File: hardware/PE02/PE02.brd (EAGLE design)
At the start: 25.4 x 27.3 mm, 28 parts, among them IC1 MSP430G2231, IC2 TPS78222, J1 78171-0002

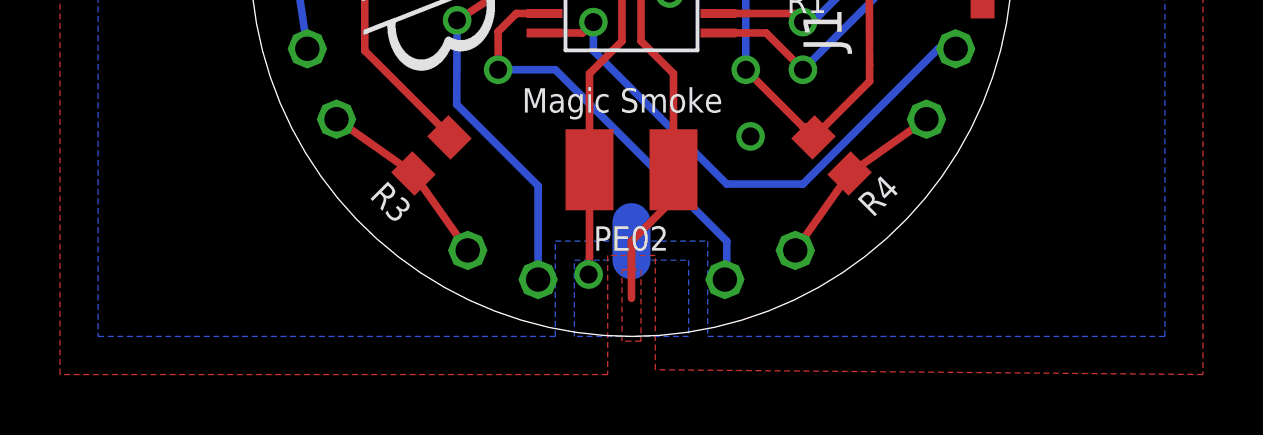
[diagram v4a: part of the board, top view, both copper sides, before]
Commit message: fixed stop mask on battery tab pads
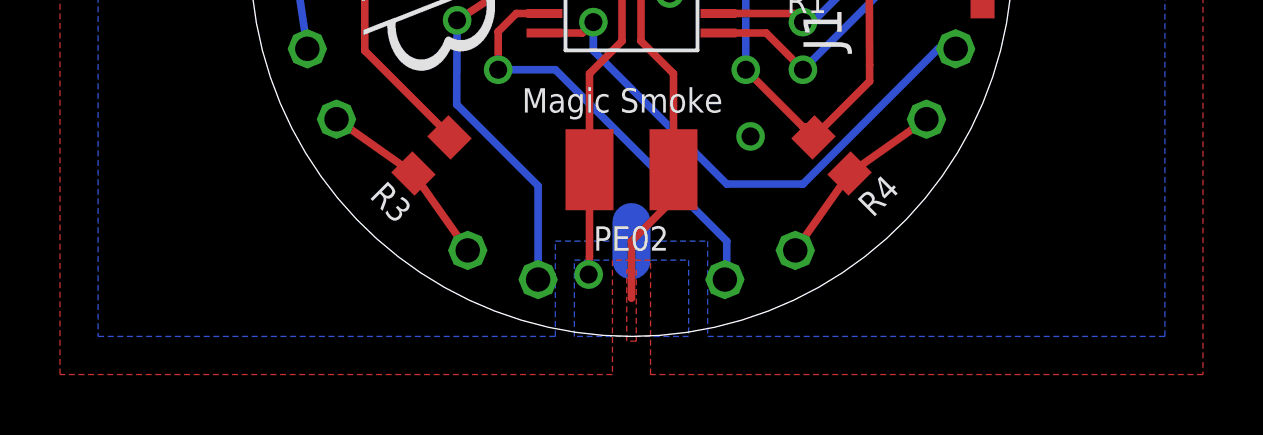
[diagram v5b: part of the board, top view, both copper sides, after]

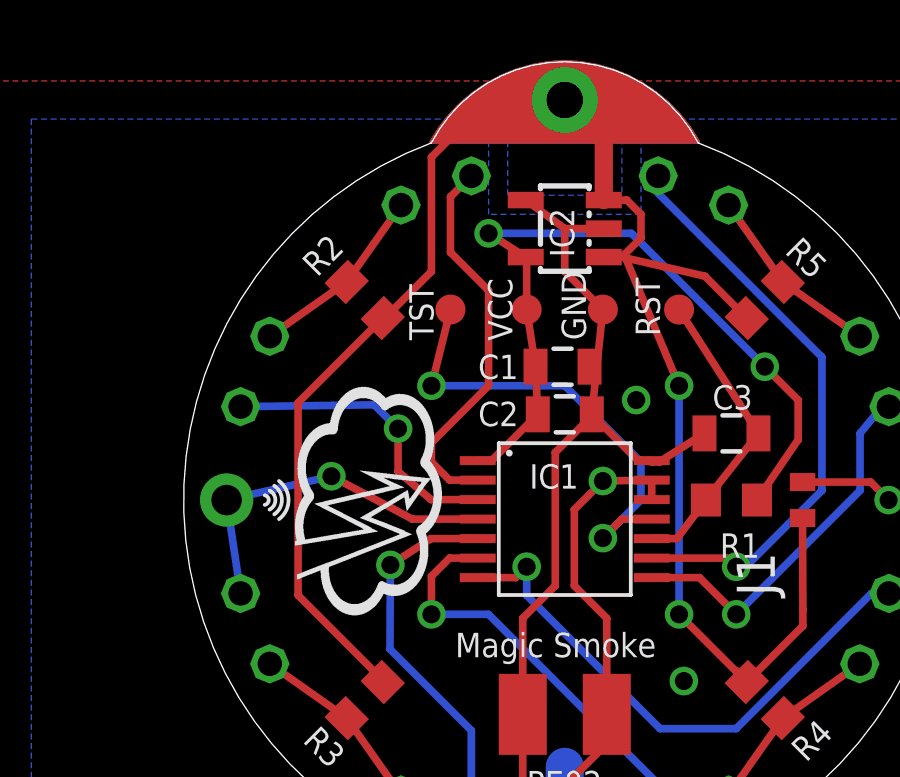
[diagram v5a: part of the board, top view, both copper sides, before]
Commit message: removed sewtab, buzzer hole
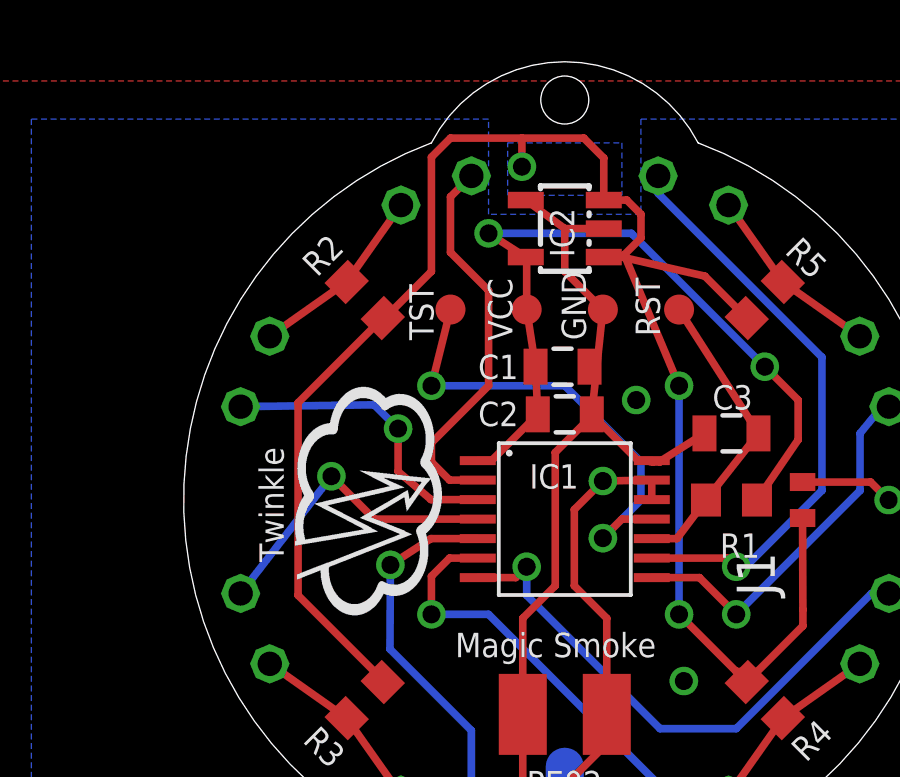
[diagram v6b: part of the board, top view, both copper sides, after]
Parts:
- removed JP1: BUZZER, adafruit:1X01-CLEANBIG
- removed TP1, TP2: SEWTAP0.4IN, adafruit:SEWINGTAP_0.4
- moved U$1 0.32 mm to (50.8, 48.6)
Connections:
- removed net N$6: D3.K, IC1.4, JP1.1
- new net N$7: D3.K, IC1.4
- net V+: no longer TP1.TAP, TP2.TAP
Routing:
- net N$6: track 12.0 -> 0.00 mm, vias 1 -> 0
- net N$7: track 0.00 -> 10.4 mm, vias 0 -> 1
- net V+: track 60.6 -> 60.1 mm, vias 2 -> 3
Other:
- board text added: "Twinkle"
- board text removed: "Magic"
- board text removed: "Smoke"
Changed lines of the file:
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@@
 <plain>
 <circle x="50.8" y="55.88" radius="11.43" width="0.0254" layer="48"/>
-<wire x1="40.79875" y1="55.72125" x2="40.79875" y2="56.03875" width="0.127" layer="21" curve="160"/>
-<wire x1="40.9575" y1="55.5625" x2="40.9575" y2="56.1975" width="0.127" layer="21" curve="126.869898"/>
-<wire x1="41.11625" y1="55.40375" x2="41.11625" y2="56.35625" width="0.127" layer="21" curve="112.619865"/>
-<wire x1="41.275" y1="55.245" x2="41.275" y2="56.515" width="0.127" layer="21" curve="106.260205"/>
 <text x="47.14875" y="50.64125" size="0.8128" layer="21" font="vector" ratio="15">Magic Smoke</text>
-<text x="59.3725" y="62.07125" size="0.8128" layer="22" font="vector" ratio="15" rot="MR45">Magic</text>
-<text x="44.60875" y="64.4525" size="0.8128" layer="22" font="vector" ratio="15" rot="MR315">Smoke</text>
 <text x="54.9275" y="50.64125" size="0.8128" layer="22" font="vector" ratio="15" rot="MR0">CC BY-SA 3.0</text>
 <circle x="50.8" y="55.88" radius="9.939321875" width="0.0254" layer="52"/>
@@
 <rectangle x1="50.32375" y1="43.4975" x2="51.27625" y2="45.56125" layer="29"/>
 <rectangle x1="48.73625" y1="43.4975" x2="52.86375" y2="45.87875" layer="30"/>
-<rectangle x1="48.73625" y1="65.88125" x2="52.86375" y2="67.6275" layer="30"/>
 <text x="54.61" y="57.62625" size="0.8128" layer="22" font="vector" ratio="15" rot="MR0">Magic Smoke</text>
 <rectangle x1="50.50491875" y1="59.3374" x2="50.78431875" y2="59.3501" layer="22" rot="R180"/>
@@
 <rectangle x1="52.16861875" y1="64.2269" x2="52.32101875" y2="64.2396" layer="22" rot="R180"/>
 <rectangle x1="51.54631875" y1="64.2269" x2="51.81301875" y2="64.2396" layer="22" rot="R180"/>
+<hole x="50.8" y="69.215" drill="1.6"/>
+<text x="41.43375" y="53.81625" size="0.8128" layer="21" font="vector" ratio="15" rot="R90">Twinkle</text>
+<rectangle x1="48.73625" y1="65.88125" x2="52.86375" y2="67.945" layer="30"/>
 </plain>
 <attributes>
@@
 </element>
 <element name="D2" library="dp_devices" package="LED-3MM" value="395nm" x="40.48125" y="60.16625" smashed="yes" rot="MR292.5">
-<attribute name="NAME" x="42.098990625" y="58.393309375" size="0.8128" layer="26" font="vector" ratio="15" rot="MR112.5"/>
+<attribute name="NAME" x="42.257740625" y="58.234559375" size="0.8128" layer="26" font="vector" ratio="15" rot="MR112.5"/>
 </element>
 <element name="D1" library="dp_devices" package="LED-3MM" value="395nm" x="46.51375" y="66.19875" smashed="yes" rot="MR157.5">
@@
 </element>
 <element name="D8" library="dp_devices" package="LED-3MM" value="395nm" x="55.08625" y="66.19875" smashed="yes" rot="MR22.5">
-<attribute name="NAME" x="53.355784375" y="64.4677875" size="0.8128" layer="26" font="vector" ratio="15" rot="MR202.5"/>
+<attribute name="NAME" x="53.673284375" y="64.3090375" size="0.8128" layer="26" font="vector" ratio="15" rot="MR202.5"/>
 </element>
 <element name="D7" library="dp_devices" package="LED-3MM" value="395nm" x="61.11875" y="60.16625" smashed="yes" rot="MR247.5">
@@
 </element>
 <element name="D6" library="dp_devices" package="LED-3MM" value="395nm" x="61.11875" y="51.59375" smashed="yes" rot="MR112.5">
-<attribute name="NAME" x="59.3422625" y="53.2079375" size="0.8128" layer="26" font="vector" ratio="15" rot="MR292.5"/>
+<attribute name="NAME" x="59.3422625" y="53.3666875" size="0.8128" layer="26" font="vector" ratio="15" rot="MR292.5"/>
 </element>
 <element name="D5" library="dp_devices" package="LED-3MM" value="395nm" x="55.08625" y="45.56125" smashed="yes" rot="MR337.5">
-<attribute name="NAME" x="54.609209375" y="47.882984375" size="0.8128" layer="26" font="vector" ratio="15" rot="MR337.5"/>
+<attribute name="NAME" x="54.767959375" y="47.882984375" size="0.8128" layer="26" font="vector" ratio="15" rot="MR337.5"/>
 </element>
 <element name="IC2" library="v-reg-3" package="SOT23-5" value="TPS78222" x="50.8" y="64.92875" smashed="yes" rot="R90">
@@
 <attribute name="NAME" x="51.508046875" y="61.210071875" size="0.8128" layer="25" font="vector" ratio="15" rot="R90"/>
 </element>
-<element name="U$1" library="SparkFun" package="OSHW-LOGO-S" value="" x="50.8" y="48.895" rot="MR0"/>
-<element name="TP1" library="adafruit" package="SEWINGTAP_0.4" value="SEWTAP0.4IN" x="50.8" y="69.215"/>
-<element name="TP2" library="adafruit" package="SEWINGTAP_0.4" value="SEWTAP0.4IN" x="50.8" y="69.215" rot="MR0"/>
-<element name="JP1" library="adafruit" package="1X01-CLEANBIG" value="BUZZER" x="39.52875" y="55.88" smashed="yes"/>
+<element name="U$1" library="SparkFun" package="OSHW-LOGO-S" value="" x="50.8" y="48.5775" rot="MR0"/>
 <element name="MVS0608.02" library="rcl" package="R1210" value="VIBRATION SENSOR" x="50.8" y="48.73625" smashed="yes"/>
 <element name="C1" library="SparkFun" package="0805" value="1uF" x="50.725809375" y="60.325" smashed="yes">
@@
 <wire x1="46.34" y1="54.595" x2="44.987096875" y2="53.71833125" width="0.254" layer="1"/>
 </signal>
-<signal name="N$6">
-<contactref element="IC1" pad="4"/>
-<contactref element="D3" pad="K"/>
-<wire x1="47.8999" y1="55.245" x2="45.72" y2="55.245" width="0.254" layer="1"/>
-<wire x1="45.72" y1="55.245" x2="43.02125" y2="56.67375" width="0.254" layer="1"/>
-<via x="43.02125" y="56.67375" extent="1-16" drill="0.6" shape="square"/>
-<contactref element="JP1" pad="1"/>
-<wire x1="39.52875" y1="55.88" x2="39.99524375" y2="52.767075" width="0.254" layer="16"/>
-<wire x1="39.52875" y1="55.88" x2="43.02125" y2="56.67375" width="0.254" layer="16"/>
-</signal>
 <signal name="N$8">
 <contactref element="IC1" pad="2"/>
@@
 <wire x1="41.91" y1="52.705" x2="44.733540625" y2="49.881459375" width="0.254" layer="1"/>
 <wire x1="44.733540625" y1="49.881459375" x2="44.733540625" y2="49.813540625" width="0.254" layer="1"/>
-<contactref element="TP1" pad="TAP"/>
 <wire x1="44.733540625" y1="61.94645625" x2="44.80145625" y2="61.94645625" width="0.254" layer="1"/>
 <wire x1="44.80145625" y1="61.94645625" x2="46.355" y2="63.5" width="0.254" layer="1"/>
 <wire x1="46.355" y1="63.5" x2="46.355" y2="67.31" width="0.254" layer="1"/>
-<wire x1="46.355" y1="67.31" x2="47.625" y2="68.58" width="0.254" layer="1"/>
-<wire x1="47.625" y1="68.58" x2="50.165" y2="68.58" width="0.254" layer="1"/>
-<wire x1="50.165" y1="68.58" x2="50.8" y2="69.215" width="0.254" layer="1"/>
+<wire x1="46.355" y1="67.31" x2="46.99" y2="67.945" width="0.254" layer="1"/>
 <wire x1="41.91" y1="59.122915625" x2="44.733540625" y2="61.94645625" width="0.254" layer="1"/>
-<wire x1="52.1001" y1="65.87875" x2="52.1001" y2="67.9149" width="0.6096" layer="1"/>
-<wire x1="52.1001" y1="67.9149" x2="50.8" y2="69.215" width="0.254" layer="1"/>
 <polygon width="0.254" layer="16">
 <vertex x="48.895" y="66.04"/>
-<vertex x="48.895" y="69.85"/>
-<vertex x="52.705" y="69.85"/>
+<vertex x="48.895" y="67.78625"/>
+<vertex x="52.705" y="67.78625"/>
 <vertex x="52.705" y="66.04"/>
 </polygon>
-<contactref element="TP2" pad="TAP"/>
 <via x="54.61" y="59.69" extent="1-16" drill="0.6" shape="square"/>
 <wire x1="54.61" y1="59.69" x2="52.783125" y2="64.056875" width="0.254" layer="1"/>
@@
 <wire x1="58.7375" y1="52.22875" x2="58.7375" y2="51.684584375" width="0.254" layer="1"/>
 <wire x1="58.7375" y1="51.684584375" x2="56.86645625" y2="49.813540625" width="0.254" layer="1"/>
+<wire x1="52.1001" y1="65.87875" x2="52.1001" y2="67.2799" width="0.254" layer="1"/>
+<wire x1="52.1001" y1="67.2799" x2="51.435" y2="67.945" width="0.254" layer="1"/>
+<wire x1="51.435" y1="67.945" x2="49.37125" y2="67.945" width="0.254" layer="1"/>
+<via x="49.37125" y="66.9925" extent="1-16" drill="0.6" shape="square"/>
+<wire x1="49.37125" y1="67.945" x2="46.99" y2="67.945" width="0.254" layer="1"/>
+<wire x1="49.37125" y1="66.9925" x2="49.37125" y2="67.945" width="0.254" layer="1"/>
 </signal>
 <signal name="N$12">
@@
 <wire x1="44.45" y1="59.055" x2="39.99524375" y2="58.992921875" width="0.254" layer="16"/>
 </signal>
+<signal name="N$7">
+<contactref element="IC1" pad="4"/>
+<contactref element="D3" pad="K"/>
+<via x="43.02125" y="56.67375" extent="1-16" drill="0.6" shape="square"/>
+<wire x1="47.8999" y1="55.245" x2="44.45" y2="55.245" width="0.254" layer="1"/>
+<wire x1="44.45" y1="55.245" x2="43.02125" y2="56.67375" width="0.254" layer="1"/>
+<wire x1="39.99524375" y1="52.767075" x2="43.02125" y2="56.67375" width="0.254" layer="16"/>
+</signal>
 </signals>

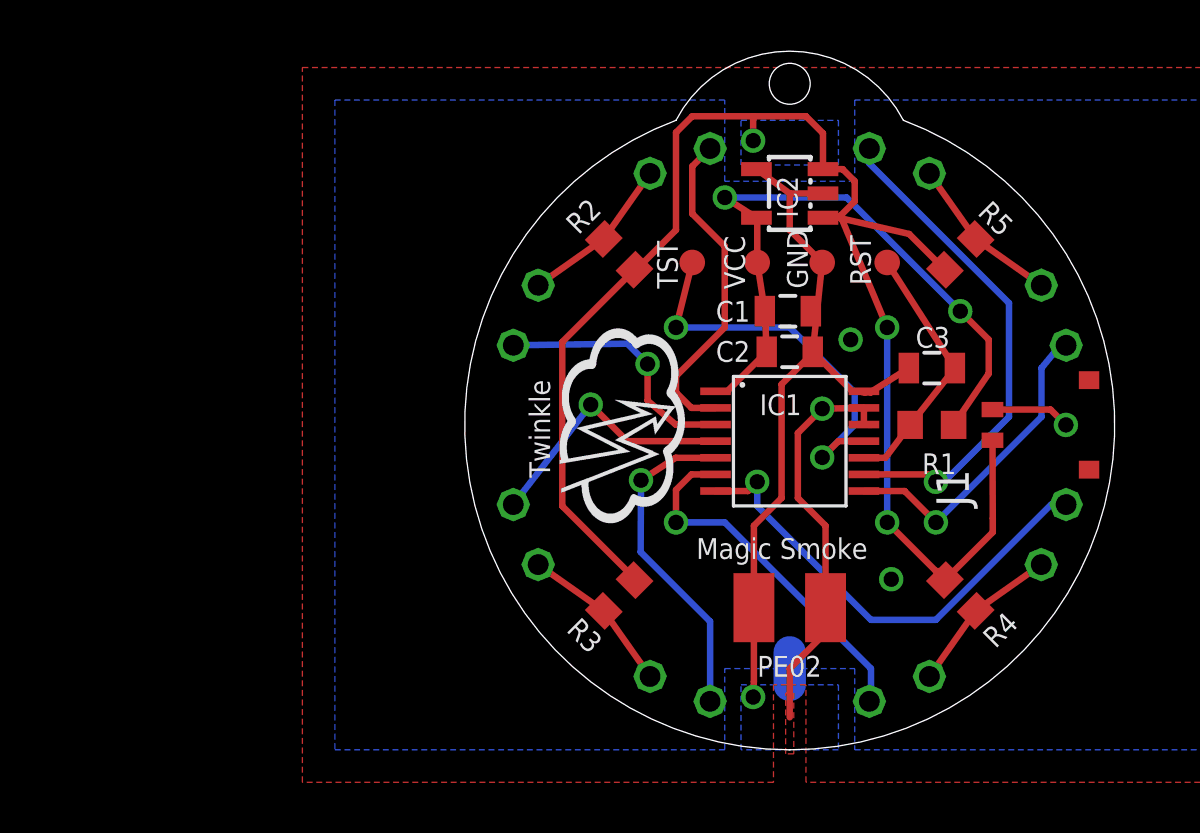
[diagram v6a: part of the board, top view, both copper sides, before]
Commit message: Added piezo buzzer circuit
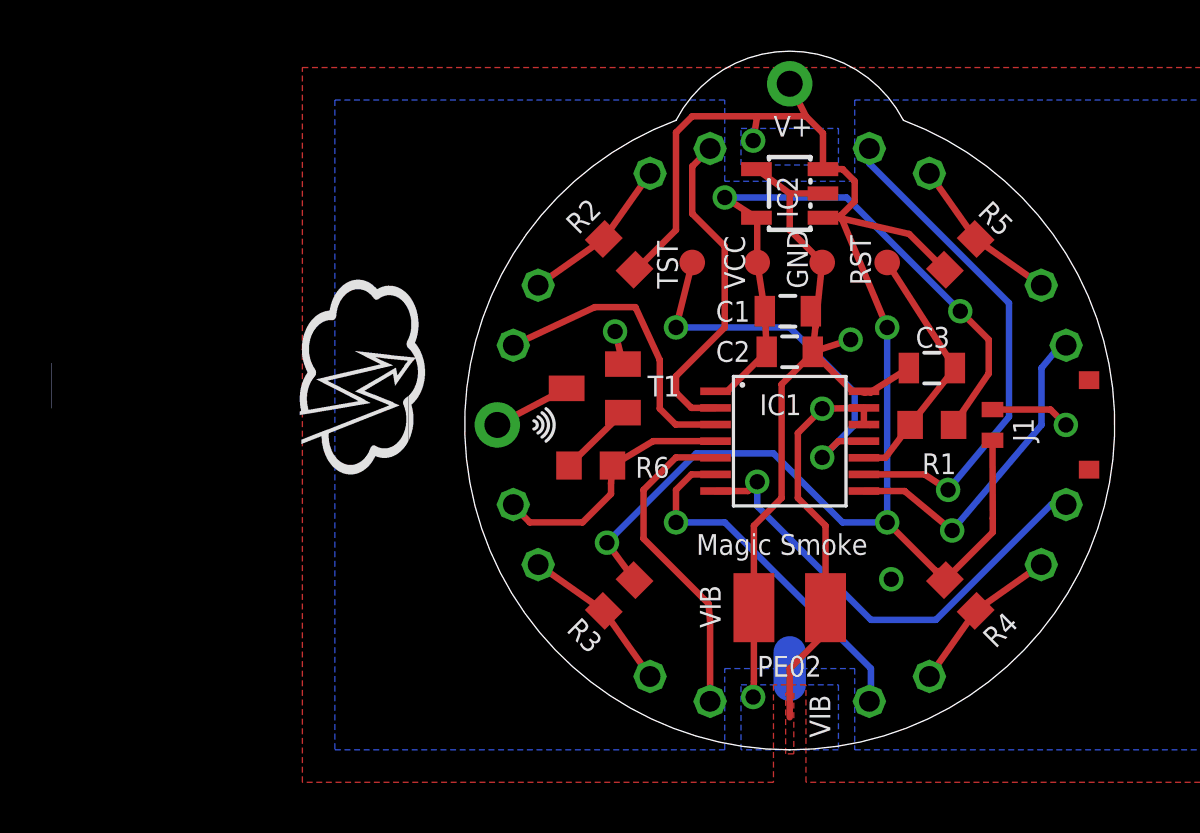
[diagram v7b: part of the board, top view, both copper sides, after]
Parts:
- added JP1, JP2: (no value), adafruit:1X01-CLEANBIG
- added R6: 1K, rcl:R0603
- added T1: BC846, transistor:SOT23
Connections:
- new net BUZZER: JP1.1, T1.3
- new net N$9: R6.1, T1.1
- net GND: now also T1.2
- net N$7: now also R6.2
- net V+: now also JP2.1
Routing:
- net GND: track 33.2 -> 36.7 mm, vias 4 -> 5
- net BUZZER: track 0.00 -> 3.06 mm
- net N$9: track 0.00 -> 2.95 mm
- net V+: track 60.1 -> 62.5 mm, vias 3 -> 4
- net N$12: track 10.0 -> 11.7 mm, vias 1 -> 0
- net N$4: track 12.4 -> 13.0 mm
- net N$7: track 10.4 -> 10.0 mm, vias 1 -> 0
- net N$5: track 12.9 -> 12.7 mm, vias 1 -> 0
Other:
- board text added: "V+"
- board text added: "VIB"
- board text removed: "Twinkle"
